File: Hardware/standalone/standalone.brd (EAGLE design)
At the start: 100 x 80 mm, 94 parts, among them IC1 STM32F050C6T6A, IC2 AP1212, Q2 32.768khz, U1 NMOS_2N7002, U10 ZXCT1107SA-7, U2 DMS3016SSS-13, U3 DMS3016SSS-13, U4 LM2576S, U5 NMOS_2N7002, U6 NMOS_2N7002, U7 INA213AIDCKT, U9 PMOS_RSS090P03, X1 KUSBVX, X2 KUSBVX

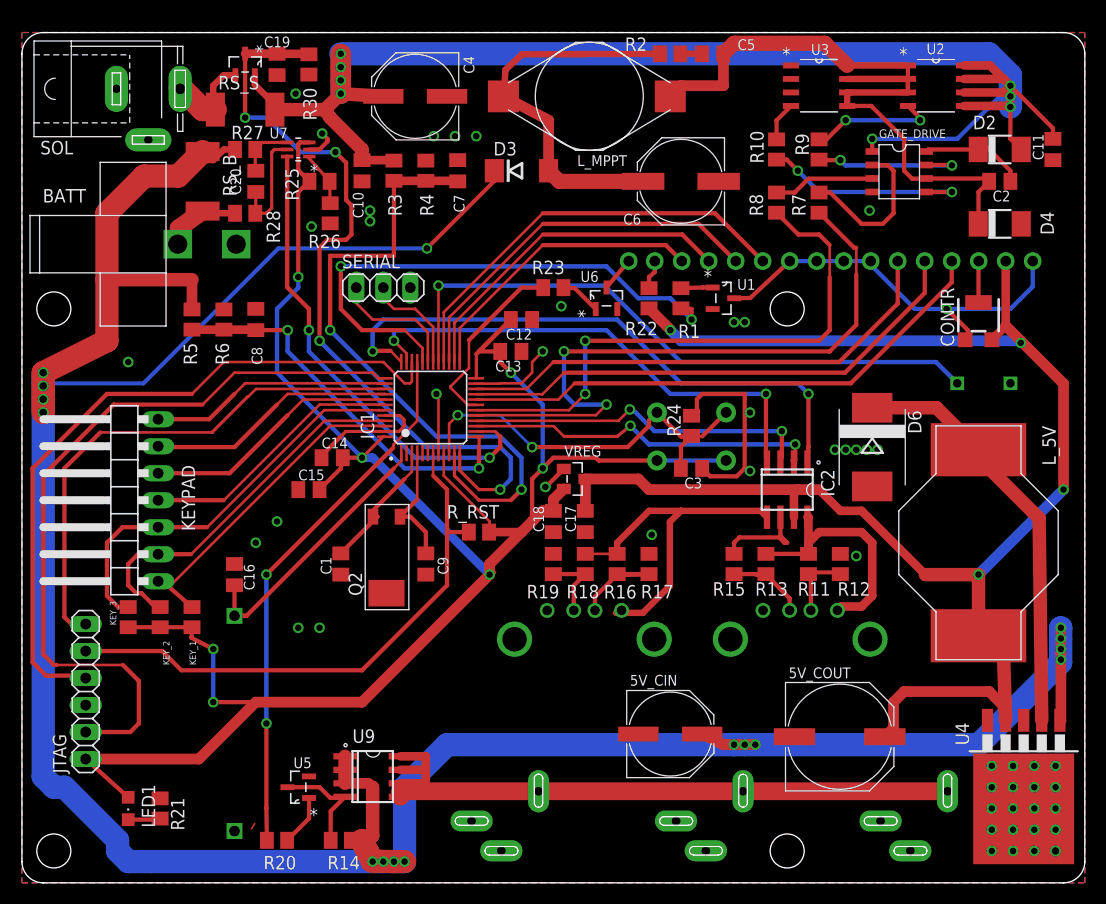
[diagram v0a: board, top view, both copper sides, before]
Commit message: Removed Keypad Pullups and Fixed MPPT out tracks
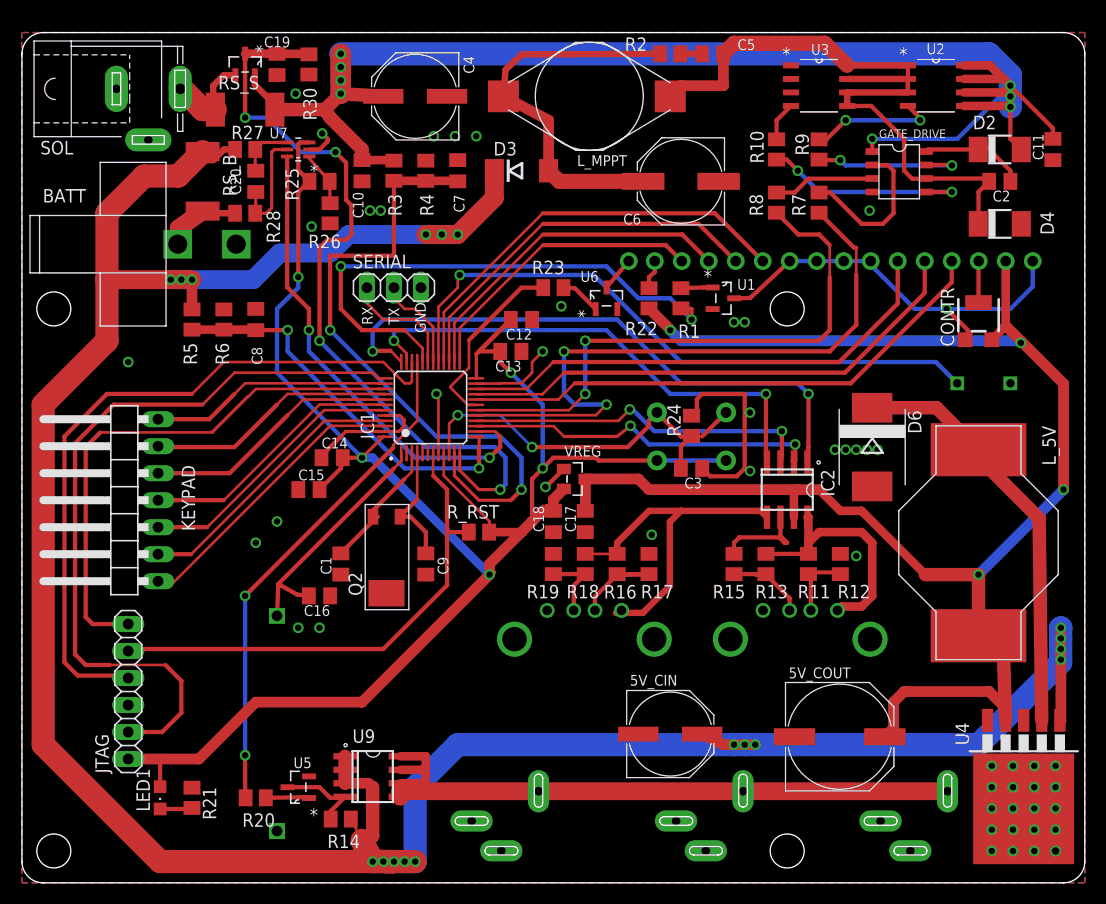
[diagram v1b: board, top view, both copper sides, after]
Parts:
- removed KEY_1, KEY_2, KEY_3: 10K, rcl:M0805
- moved C16 8.25 mm to (28.0, 27.0), turned to 180 degrees
- moved R20 4.47 mm to (22.0, 8.00)
- moved BATT_BCKUP 4.00 mm to (24.0, 15.0)
- moved JTAG 4.00 mm to (10.0, 18.0)
- moved LED1 3.16 mm to (13.0, 8.00)
- moved R21 3.16 mm to (16.0, 8.00)
- moved R14 2.00 mm to (30.0, 6.00)
- moved SERIAL 1.00 mm to (35.0, 56.0)
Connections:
- net +3V3: no longer KEY_1.2, KEY_2.2, KEY_3.2
- net N$23: no longer KEY_1.1
- net N$24: no longer KEY_2.1
- net N$26: no longer KEY_3.1
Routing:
- net +3V3: track 205.7 -> 180.6 mm, vias 7 -> 5
- net N$26: track 38.7 -> 25.9 mm
- net V_LOAD: track 291.3 -> 281.5 mm, vias 16 -> 18
- net N$24: track 35.6 -> 26.5 mm
- net NRST: track 53.1 -> 48.0 mm
- net N$23: track 32.0 -> 28.0 mm
- net 12V_OUT_EN: track 50.9 -> 47.7 mm
- net V_BACKUP: track 26.3 -> 23.2 mm
- net N$25: track 10.5 -> 8.52 mm
- net SWO: track 49.5 -> 50.7 mm
- net GND: track 76.7 -> 75.6 mm
- net USART1_TX: track 10.1 -> 9.09 mm
- net USART1_RX: track 12.1 -> 11.1 mm
- net SWCLK: track 72.6 -> 71.8 mm
- net SOL_I: track 74.7 -> 74.0 mm
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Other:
- board text added: "GND"
- board text added: "Move these to below USB"
- board text added: "RX"
- board text added: "TX"
- board text removed: "MPPT OUTPUT TRACK NOT BIG ENOUGH"

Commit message: Updated MPPT Inductor and added comments
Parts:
- 5V_CIN: value 100u -> 100uF
- C5: value 0.1uF -> 100nF
- D3: value (none) -> SSB43L
- D4: value US1D - 1625280 -> US1D
- R21: value 1K -> 1k
- U2, U3: value DMS3016SSS-13 -> FDS6690a
- moved C5 3.00 mm to (68.0, 78.0)
- moved R2 3.00 mm to (64.0, 78.0)
- moved D3 2.00 mm to (47.0, 65.0)
- moved C6 1.41 mm to (63.0, 65.0)
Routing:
- net N$12: track 36.5 -> 41.3 mm
- net V_LOAD: track 281.5 -> 279.6 mm

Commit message: Hardware fixes
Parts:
- removed C16: 1uF, resistor:C0805K
- added R29: 1k, resistor:M0805
- added U8: NMOS_2N7002, equinox:SOT103P240X110-3N
- R4, R6: value 1.32k -> 1.33k
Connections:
- new net N$42: BUZZ1.P$2, U8.3
- new net N$43: R29.2, U8.1
- net GND: now also U8.2; no longer BUZZ1.P$2, C16.1
- net N$22: now also R29.1; no longer BUZZ1.P$1
- net V_BACKUP: no longer C16.2
- net V_LOAD: now also BUZZ1.P$1
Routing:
- net V_LOAD: track 279.6 -> 310.3 mm, vias 18 -> 19
- net N$42: track 0.00 -> 8.82 mm
- net N$22: track 60.0 -> 56.1 mm, vias 1 -> 2
- net N$43: track 0.00 -> 3.44 mm
- net V_BACKUP: track 23.2 -> 20.1 mm

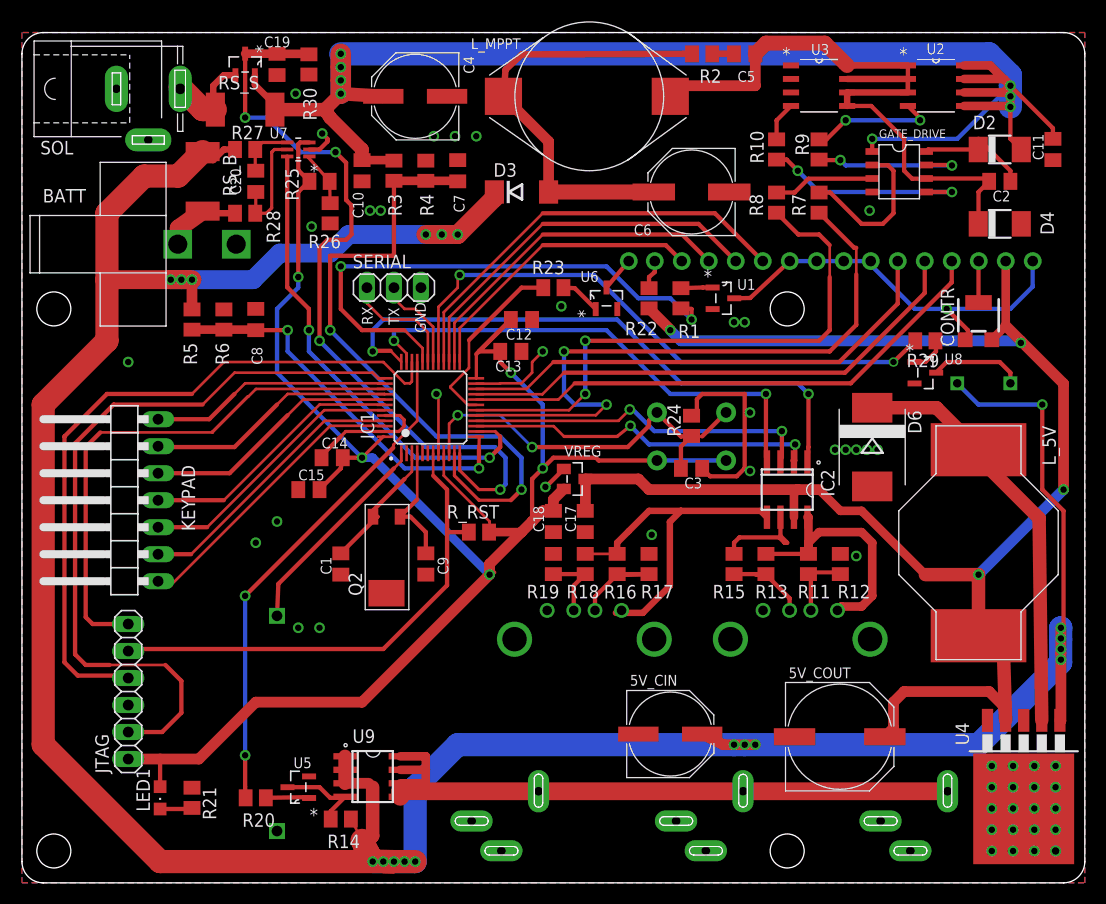
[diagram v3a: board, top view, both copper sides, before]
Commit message: Moved drill holes to correct position
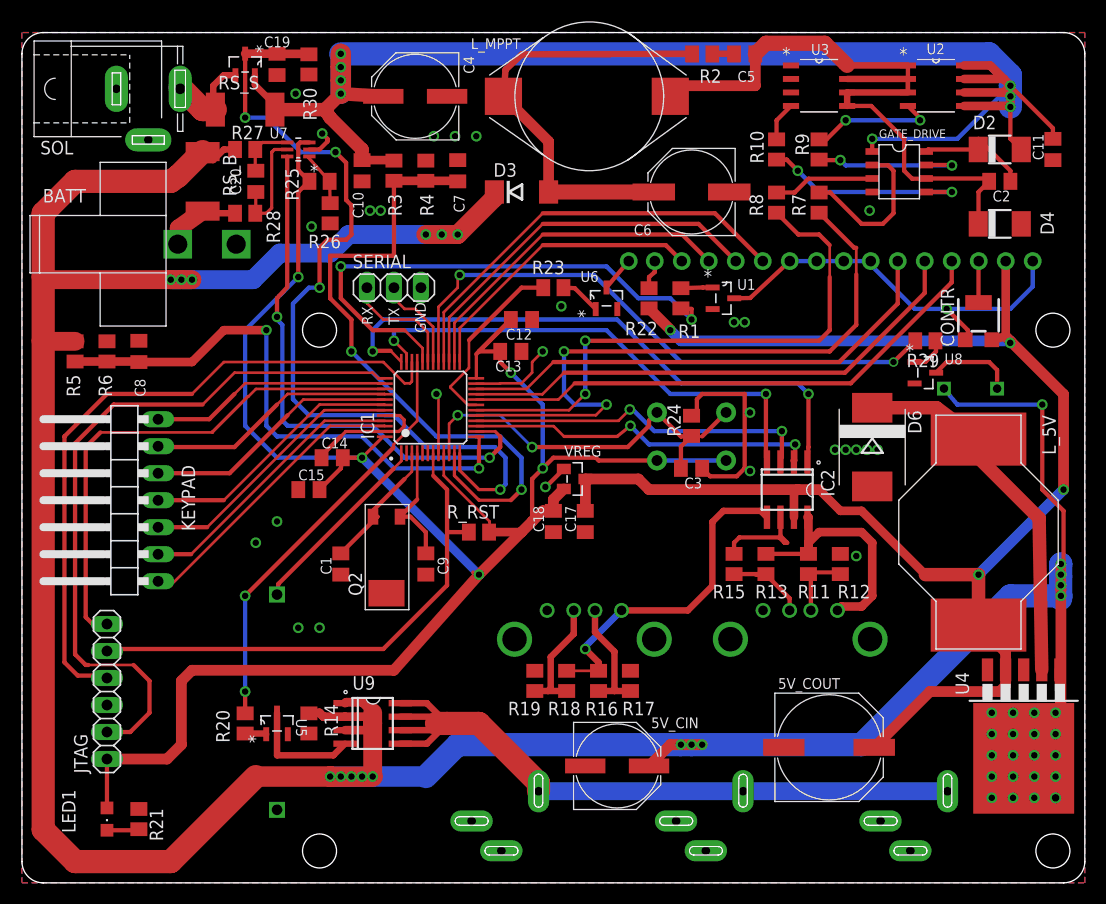
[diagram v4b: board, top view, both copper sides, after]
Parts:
- BUZZ1: device buzzer:14MM_5M_PINS -> equinox:BUZZ_14MM_5M_PINS
- moved C8 11.4 mm to (11.0, 50.0)
- moved R5 11.4 mm to (5.00, 50.0)
- moved R6 11.4 mm to (8.00, 50.0)
- moved R16 11.1 mm to (54.2, 19.0)
- moved R17 11.1 mm to (57.2, 19.0)
- moved R18 11.1 mm to (51.2, 19.0)
- moved R19 11.1 mm to (48.2, 19.0)
- moved R14 9.49 mm to (27.0, 15.0), turned to 90 degrees
- moved R20 7.07 mm to (21.0, 15.0), turned to 270 degrees
- moved U5 6.32 mm to (24.0, 15.0), turned to 90 degrees
- moved 5V_CIN 5.83 mm to (56.0, 11.0)
- moved LED1 5.39 mm to (8.00, 6.00)
- moved R21 5.39 mm to (11.0, 6.00)
- moved U9 5.00 mm to (33.0, 15.0)
- moved U4 4.75 mm to (94.2, 14.2)
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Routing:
- net BATT_V: track 36.8 -> 53.2 mm
- net +3V3: track 180.6 -> 194.1 mm
- net V_LOAD: track 310.3 -> 320.9 mm
- net 12V_OUT_EN: track 47.7 -> 39.8 mm
- net SOL_I: track 74.0 -> 81.4 mm
- net 12V_OUT: track 62.5 -> 69.1 mm
- net BATT_I: track 45.2 -> 51.2 mm
- net +5V: track 152.3 -> 147.3 mm
- net N$21: track 41.2 -> 36.3 mm
- net N$36: track 6.86 -> 11.6 mm
- net SWCLK: track 71.8 -> 67.8 mm
- net N$25: track 8.52 -> 10.9 mm
- net N$35: track 4.15 -> 2.01 mm
- net SWO: track 50.7 -> 48.7 mm
- net SWDIO: track 66.2 -> 64.2 mm
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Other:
- board text removed: "Move these to below USB"

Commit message: Latest V2.4 PCB design (Sent to EuroCircuits)
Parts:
- removed R1: 1k, resistor:M0805
- removed U1: NMOS_2N7002, equinox:SOT103P240X110-3N
- added C16: 1uF, resistor:C0805K
- added D1: SSB43L, equinox:DO214AA
- added D5: BZX384-C3V6, equinox:SOD323
- added PTC1: 7A, equinox:PTC_MF_R700
- added R31: 10M, resistor:M0805
- added U11, U12: NMOS_2N7002, equinox:SOT103P240X110-3N
- moved C17 8.94 mm to (61.0, 30.0)
- moved C18 8.94 mm to (58.0, 30.0)
- moved VREG 8.06 mm to (59.0, 34.0)
- moved R5 2.75 mm to (5.00, 47.2)
- moved C8 2.15 mm to (12.2, 48.2)
- moved R6 2.02 mm to (9.00, 48.2)
- moved R30 2.00 mm to (25.0, 77.0)
- moved C19 1.75 mm to (22.2, 77.0)
- moved U10 1.50 mm to (19.5, 77.0)
- moved LED1 1.00 mm to (8.00, 7.00)
- moved R21 1.00 mm to (11.0, 7.00)
- moved R_RST 1.00 mm to (43.0, 32.0), turned to 90 degrees
- renumbered 5V_CIN to C21, 5V_COUT to C22, GATE_DRIVE to IC3, Q2 to Q1, U$2 to DC3, U$3 to DC2, U$4 to DC1
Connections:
- removed net LCD_PWR: IC1.32, R1.2
- removed net N$17: R1.1, U1.1
- removed net N$5: CONTR.1, DIS1.1, DIS1.10, DIS1.7, DIS1.8, DIS1.9, U1.3
- new net N$44: C16.2, R31.2, U11.1
- new net N$45: U11.3, U12.2
- new net N$46: BATT.P$1, PTC1.P$2
- net GND: now also C16.1, CONTR.1, D1.A, D5.A, DIS1.1, DIS1.10, DIS1.7, DIS1.8, DIS1.9, U11.2; no longer U1.2
- net N$4: now also D1.C, PTC1.P$1; no longer BATT.P$1
- net NRST: now also U12.3
- net SOL_I: now also D5.C
- net WKUP: now also R31.1, U12.1
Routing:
- net LCD_PWR: track 51.0 -> 0.00 mm, vias 2 -> 0
- net N$5: track 38.6 -> 0.00 mm, vias 1 -> 0
- net N$4: track 7.80 -> 30.9 mm
- net NRST: track 50.0 -> 72.8 mm, vias 0 -> 2
- net +3V3: track 194.1 -> 210.1 mm, vias 5 -> 4
- net N$46: track 0.00 -> 9.69 mm
- net GND: track 75.6 -> 83.5 mm, vias 47 -> 50
- net WKUP: track 37.4 -> 44.5 mm
- net N$44: track 0.00 -> 6.48 mm
- net +5V: track 147.3 -> 141.2 mm
- net SOL_I: track 81.4 -> 86.7 mm
- net N$45: track 0.00 -> 4.43 mm
- net 12V_OUT_EN: track 39.8 -> 44.0 mm
- net V_LOAD: track 320.9 -> 325.0 mm
- net N$17: track 2.99 -> 0.00 mm
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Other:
- board text added: "Designed by Ashley Grealish in London Manufactured in China"
- board text removed: "Design by Ashley Grealish - 2013"

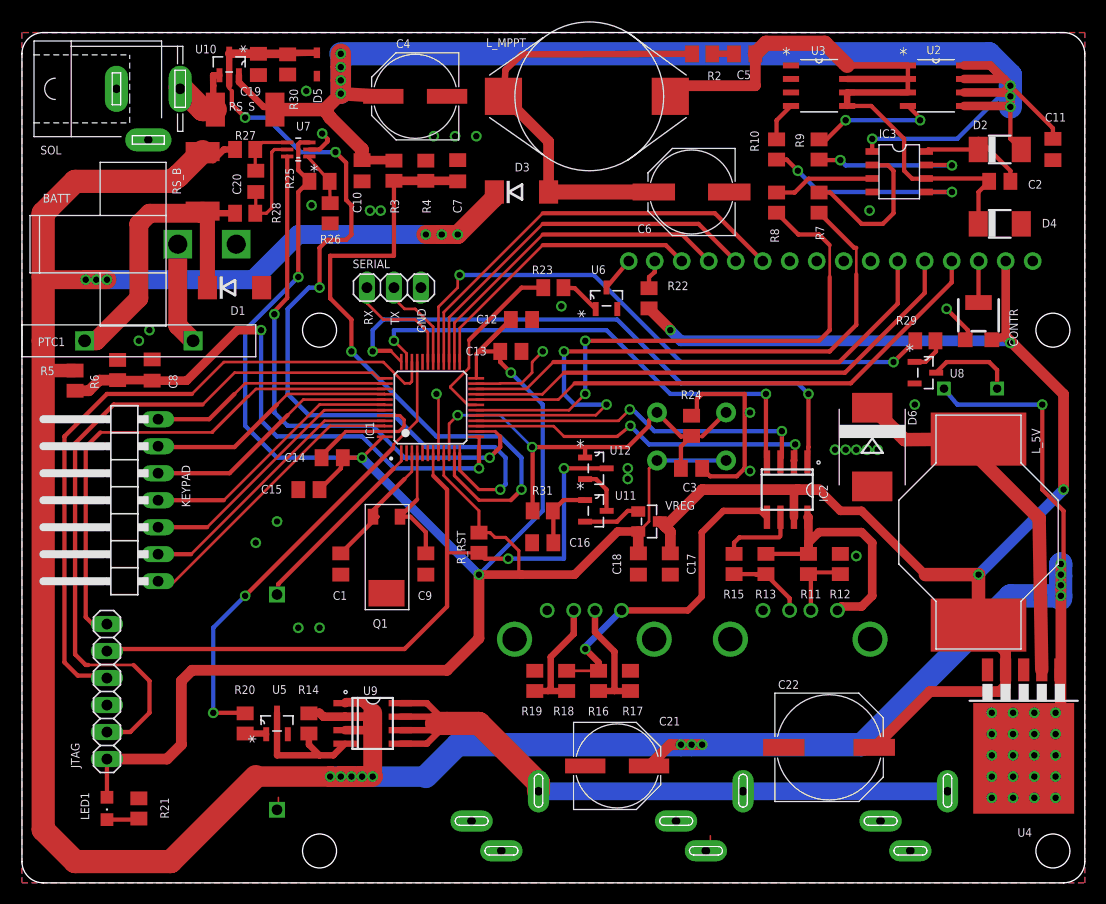
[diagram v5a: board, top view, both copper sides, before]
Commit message: Parallel Resistor added to buzzer circuit.
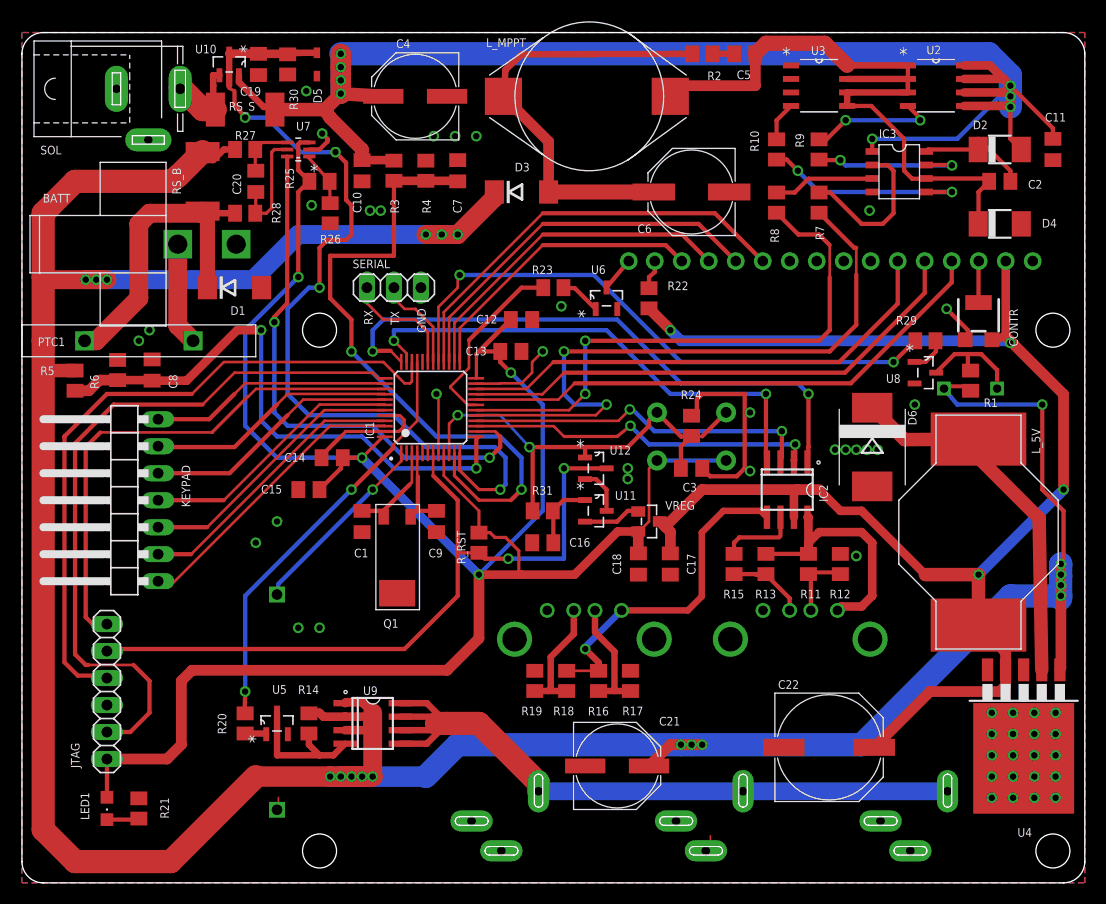
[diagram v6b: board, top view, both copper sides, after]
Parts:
- added R1: 100, resistor:M0805
- moved C1 4.47 mm to (32.0, 34.0)
- moved C9 4.12 mm to (39.0, 34.0)
- moved Q1 1.00 mm to (35.0, 31.0)
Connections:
- net N$42: now also R1.2
- net V_LOAD: now also R1.1
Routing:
- net V_LOAD: track 325.0 -> 318.2 mm
- net 12V_OUT_EN: track 44.0 -> 39.8 mm
- net N$1: track 12.8 -> 9.10 mm
- net N$18: track 11.7 -> 8.16 mm
- net N$42: track 8.22 -> 10.6 mm
- net V_BACKUP: vias 0 -> 1
